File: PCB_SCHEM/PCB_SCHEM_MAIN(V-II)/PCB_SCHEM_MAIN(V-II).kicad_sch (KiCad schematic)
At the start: 0 parts

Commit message: Schem Update
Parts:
- added U1: RP2040, Package_DFN_QFN:QFN-56-1EP_7x7mm_P0.4mm_EP3.2x3.2mm, symbol MCU_RaspberryPi:RP2040
- added U2: TPS61291DRVR, DRV0006A, symbol 2026-10-14_05-55-56:TPS61291DRVR
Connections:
- new net: U1.1 (IOVDD), U1.10 (IOVDD), U1.22 (IOVDD), U1.33 (IOVDD), U1.42 (IOVDD), U1.49 (IOVDD)
- new net: U1.23 (DVDD), U1.50 (DVDD)

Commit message: Added all the IC's, the main framework of the PCB done. Minor wiring and final touches left
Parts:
- added BT1: Battery_Cell, Package_SON:Texas_DRC0010J_ThermalVias, symbol Device:Battery_Cell
- added C1, C2: 22pf, Package_SO:SOIC-8_3.9x4.9mm_P1.27mm, symbol Device:C_Small
- added C3: 100nf, Package_SO:SOIC-8_3.9x4.9mm_P1.27mm, symbol Device:C_Small
- added D1: SS14, Diode_SMD:D_SMA, symbol Diode:SS14
- added D2: D, Diode_SMD:D_SMA, symbol Device:D
- added J1: USB_C_Receptacle_USB2.0_14P, Package_DFN_QFN:WDFN-10-1EP_3x3mm_P0.5mm_EP1.8x2.5mm, symbol Connector:USB_C_Receptacle_USB2.0_14P
- added L1: L_Ferrite_Small, Package_BGA:BGA-624_21x21mm_Layout25x25_P0.8mm, symbol Device:L_Ferrite_Small
- added R1: R, Package_DIP:DIP-8_W7.62mm, symbol Device:R
- added R2: 10K, Package_DIP:DIP-8_W7.62mm, symbol Device:R
- added R3, R4: 5K1, Package_DIP:DIP-8_W7.62mm, symbol Device:R
- added U3: LSM6DS3, Package_LGA:LGA-14_3x2.5mm_P0.5mm_LayoutBorder3x4y, symbol Sensor_Motion:LSM6DS3
- added U4, U5: MX25L3233FM1, Package_SO:JEITA_SOIC-8_3.9x4.9mm_P1.27mm, symbol Memory_Flash:MX25L3233FM1
- added Y1: Crystal, Package_SO:JEITA_SOIC-8_3.9x4.9mm_P1.27mm, symbol Device:Crystal
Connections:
- net at U2.1 (L): now also L1.2
- net 3.3V: now reaches U2.2 (VOUT)
- net 3.3V: now also U1.1 (IOVDD), U1.10 (IOVDD), U1.22 (IOVDD), U1.33 (IOVDD), U1.42 (IOVDD), U1.43 (ADC_AVDD), U1.44 (VREG_VIN), U1.48 (USB_VDD), U1.49 (IOVDD), U2.5 (VSEL), C3.2, U3.5 (VDDIO), U3.8 (VDD), U4.8 (VCC), U5.8 (VCC)
- net VIN: now reaches U2.3 (VIN)
- net VIN: now also D1.1 (K), D2.1 (K), L1.1, R1.1
- net at U2.4 (EN_BYP): now also U1.37 (GPIO25), R1.2
- net GND: now reaches U2.6 (GND)
- net GND: now also U1.3 (GPIO1), U1.57 (GND), U2.7 (PAD), BT1.2 (-), C3.1, J1.A1 (GND), J1.A12 (GND), J1.B1 (GND), J1.B12 (GND), J1.SH (SHIELD), R2.2, R3.2, R4.2, U3.6 (GND), U3.7 (GND), U4.4 (GND)
- net at U1.16 (GPIO13): now also U5.1 (~{CS})
- net at U1.17 (GPIO14): now also U5.6 (SCLK)
- net at U1.2 (GPIO0): now also U3.1 (SDO/SA0)
- net at U1.20 (XIN): now also C1.1
- net at U1.21 (XOUT): now also C2.2
- net at U1.23 (DVDD), U1.50 (DVDD): now also U1.45 (VREG_VOUT)
- net at U1.35 (GPIO23): now also U3.9 (INT2)
- net at U1.36 (GPIO24): now also U3.4 (INT1)
- net at U1.4 (GPIO2): now also U3.13 (SCL)
- net at U1.46 (USB_DM): now also J1.A7 (D-), J1.B7 (D-)
- net at U1.47 (USB_DP): now also J1.A6 (D+), J1.B6 (D+)
- net at U1.5 (GPIO3): now also U3.14 (SDA)
- net at U1.51 (QSPI_SD3): now also U4.7 (~{HOLD}/SIO3)
- net at U1.52 (QSPI_SCLK): now also U4.6 (SCLK)
- net at U1.53 (QSPI_SD0): now also U4.5 (SI/SIO0)
- net at U1.54 (QSPI_SD2): now also U4.3 (~{WP}/SIO2)
- net at U1.55 (QSPI_SD1): now also U4.2 (SO/SIO1)
- net at U1.56 (~{QSPI_SS}): now also U4.1 (~{CS})
- new net: J1.A5 (CC1), R3.1
- new net: D1.2 (A), J1.A4 (VBUS), J1.A9 (VBUS), J1.B4 (VBUS), J1.B9 (VBUS)
- new net: J1.B5 (CC2), R4.1
- new net: R2.1, U3.12 (CS)
- new net: C1.2, Y1.1
- new net: BT1.1 (+), D2.2 (A)
- new net: C2.1, Y1.2
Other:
- moved on the sheet: U1, U2

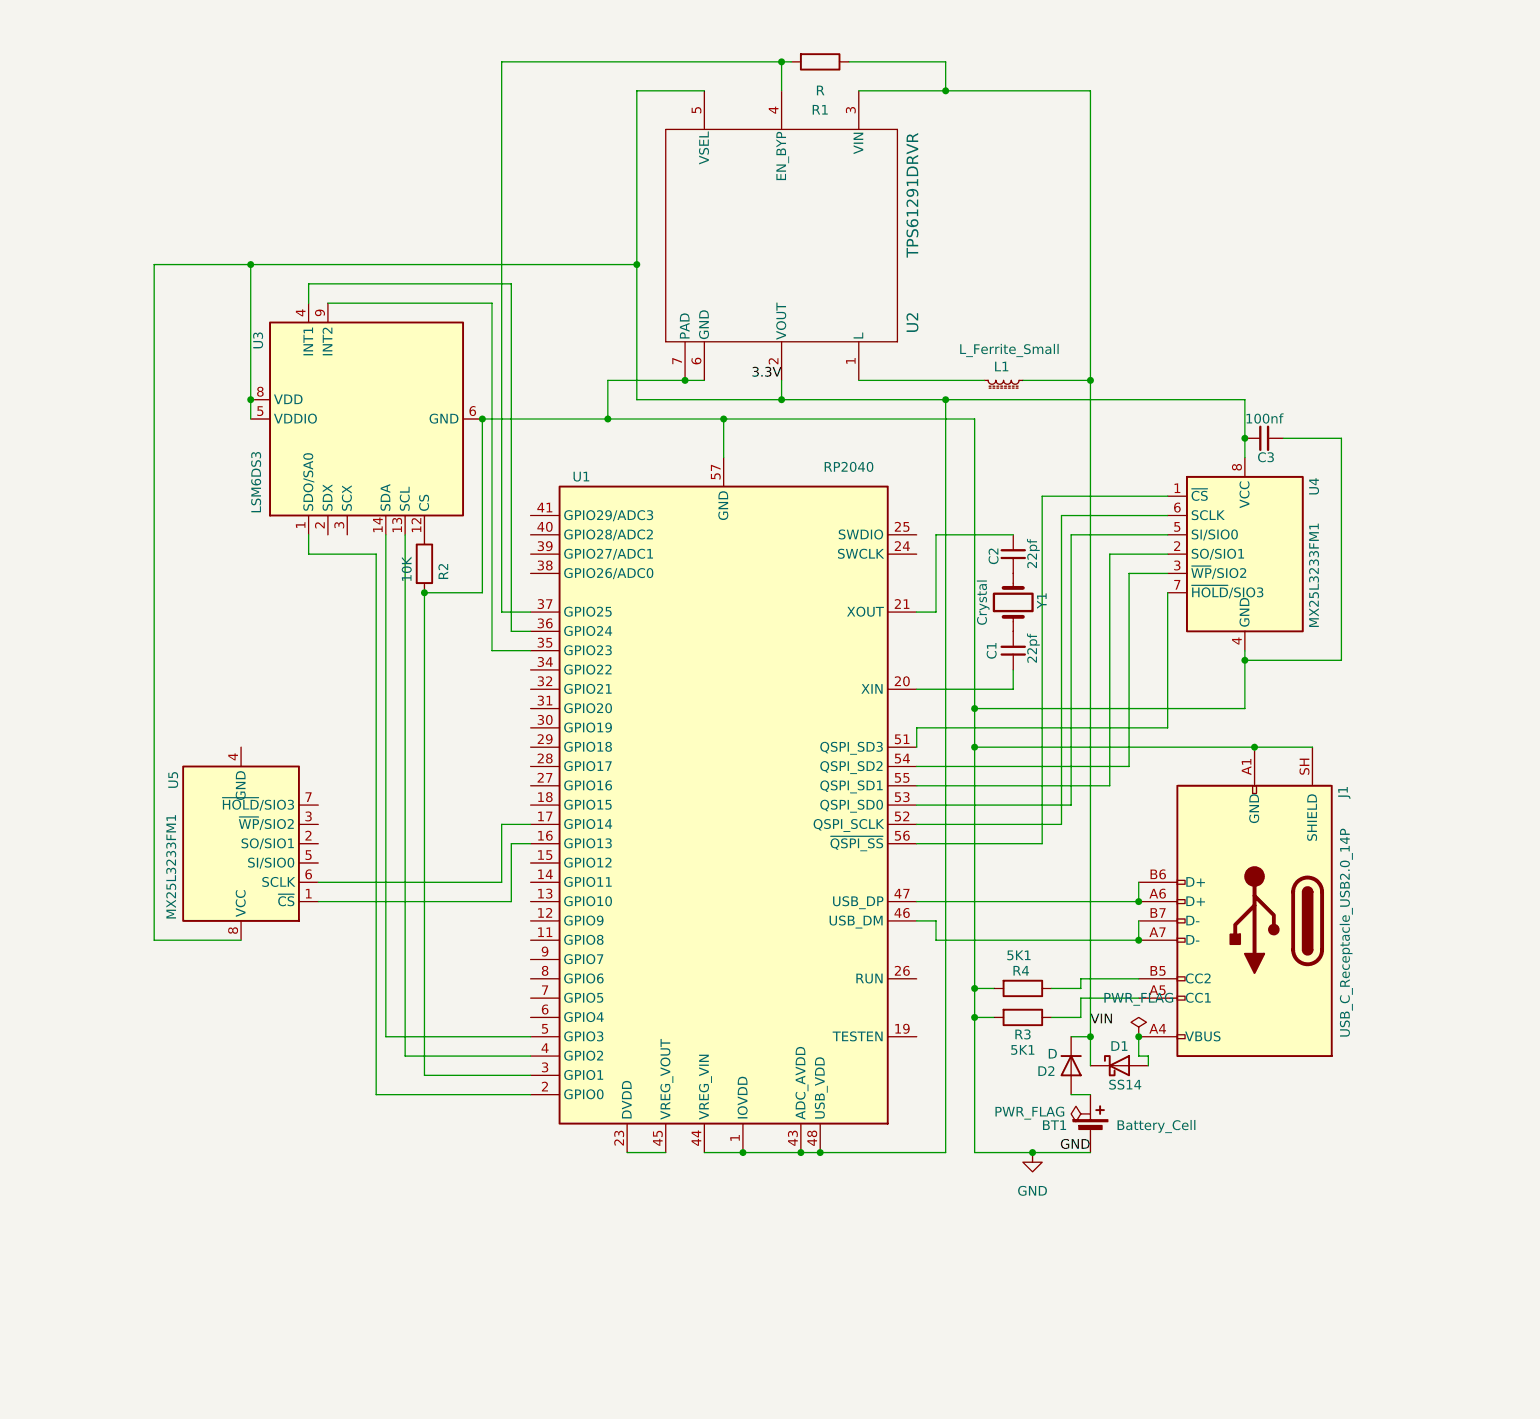
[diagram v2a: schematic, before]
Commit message: Completed Schematic design, and imported footprints to the PCB editor.
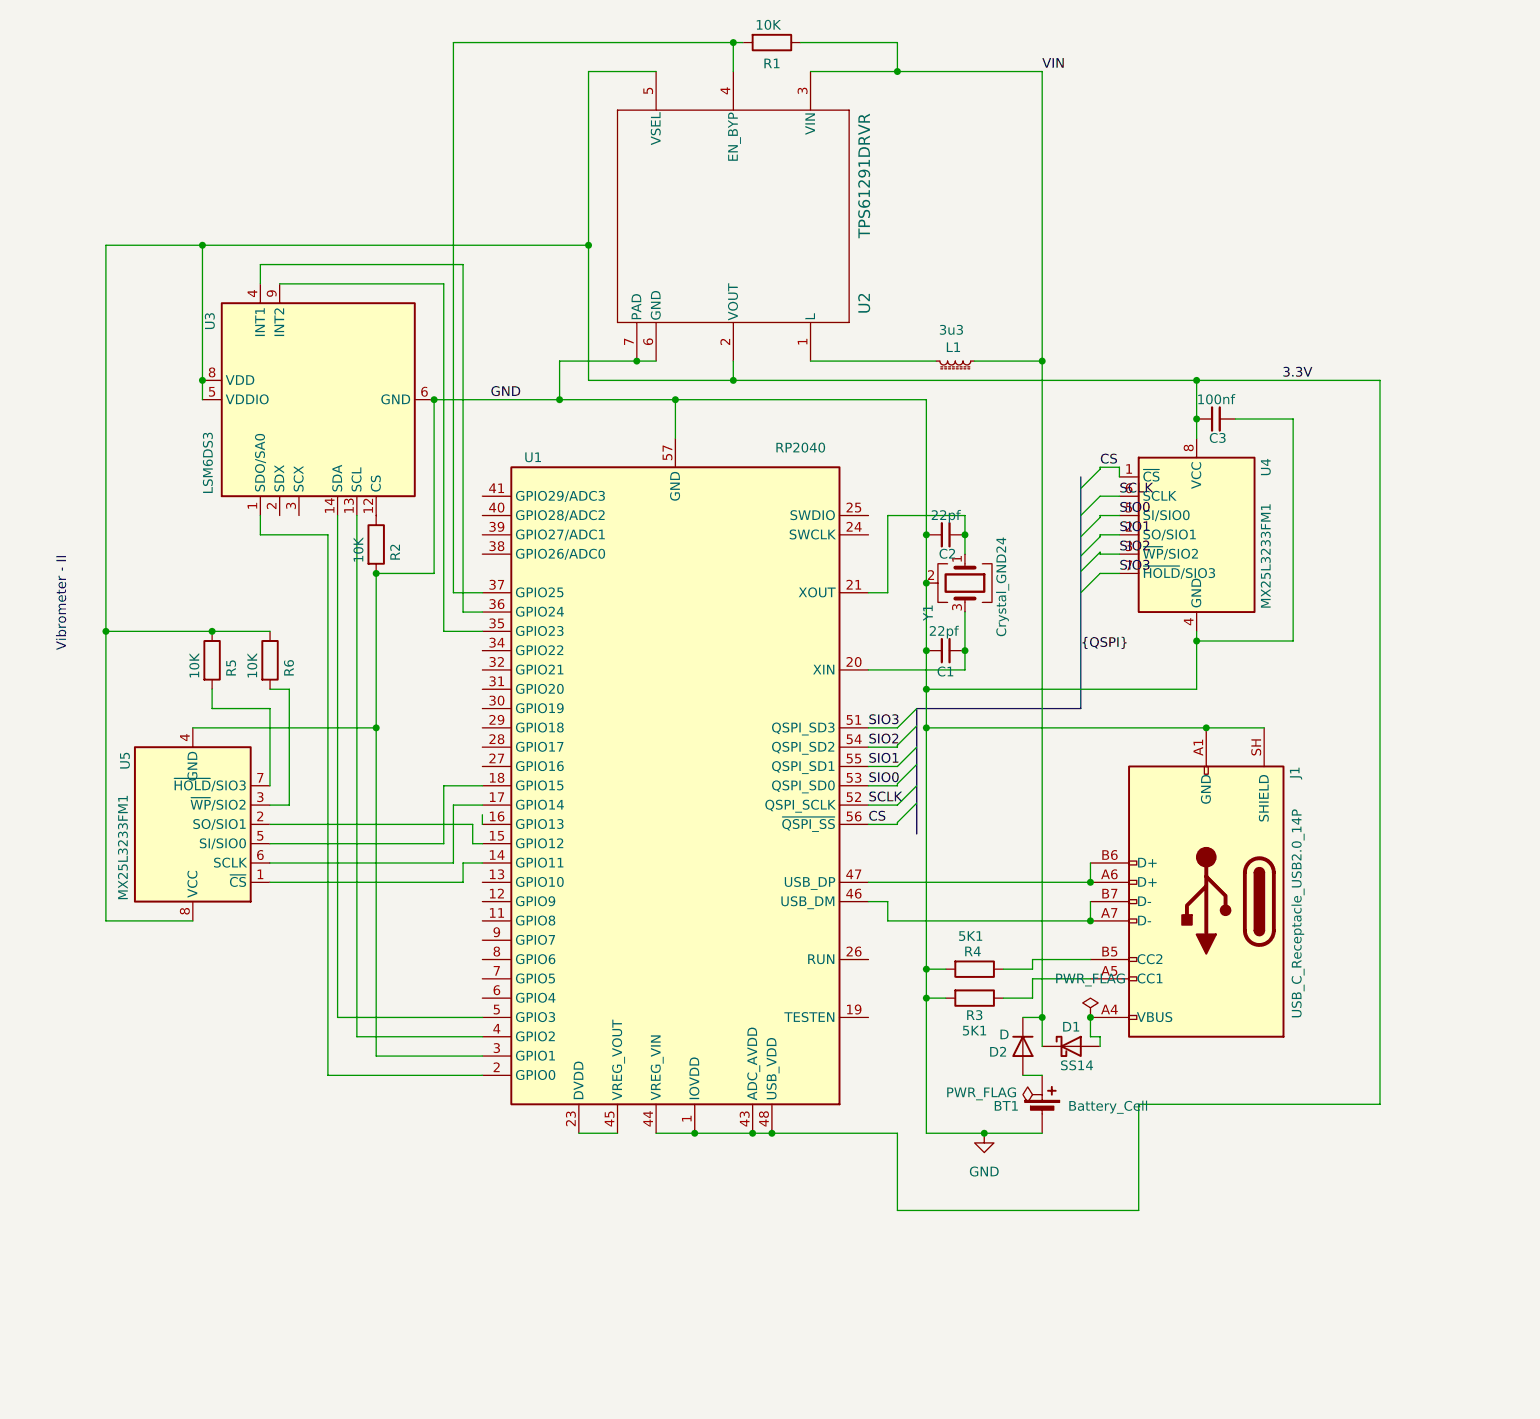
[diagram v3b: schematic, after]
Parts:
- removed Y1: Crystal, Package_SO:JEITA_SOIC-8_3.9x4.9mm_P1.27mm, symbol Device:Crystal
- added R5, R6: 10K, Resistor_SMD:R_0603_1608Metric_Pad0.98x0.95mm_HandSolder, symbol Device:R
- added Y1: Crystal_GND24, Crystal:Crystal_SMD_Abracon_ABM8AIG-4Pin_3.2x2.5mm, symbol Device:Crystal_GND24
- BT1: footprint Package_SON:Texas_DRC0010J_ThermalVias -> Battery:BatteryHolder_MYOUNG_BS-07-A1BJ001_CR2032
- C1, C2, C3: footprint Package_SO:SOIC-8_3.9x4.9mm_P1.27mm -> Capacitor_SMD:C_0603_1608Metric_Pad1.08x0.95mm_HandSolder
- J1: footprint Package_DFN_QFN:WDFN-10-1EP_3x3mm_P0.5mm_EP1.8x2.5mm -> Connector_USB:USB_C_Receptacle_GCT_USB4105-xx-A_16P_TopMnt_Horizontal
- L1: value L_Ferrite_Small -> 3u3; footprint Package_BGA:BGA-624_21x21mm_Layout25x25_P0.8mm -> Inductor_SMD:L_Coilcraft_LPS3010
- R1: value R -> 10K; footprint Package_DIP:DIP-8_W7.62mm -> Resistor_SMD:R_0603_1608Metric_Pad0.98x0.95mm_HandSolder
- R2, R3, R4: footprint Package_DIP:DIP-8_W7.62mm -> Resistor_SMD:R_0603_1608Metric_Pad0.98x0.95mm_HandSolder
- U2: footprint DRV0006A -> Package_SON:WSON-6-1EP_2x2mm_P0.65mm_EP1x1.6mm_ThermalVias
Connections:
- net 3.3V: now also R5.1, R6.1
- net GND: now also C1.2, C2.2, U5.4 (GND), Y1.2 (G), Y1.4 (G)
- net at C1.1, U1.20 (XIN): now also Y1.3
- net CS: now reaches U1.56 (~{QSPI_SS}), U4.1 (~{CS})
- net SIO1: now reaches U1.55 (QSPI_SD1), U4.2 (SO/SIO1)
- net SIO2: now reaches U1.54 (QSPI_SD2), U4.3 (~{WP}/SIO2)
- net SIO0: now reaches U1.53 (QSPI_SD0), U4.5 (SI/SIO0)
- net SCLK: now reaches U1.52 (QSPI_SCLK), U4.6 (SCLK)
- net SIO3: now reaches U1.51 (QSPI_SD3), U4.7 (~{HOLD}/SIO3)
- net at U5.1 (~{CS}): now also U1.14 (GPIO11); no longer U1.16 (GPIO13)
- net at U5.2 (SO/SIO1): now also U1.15 (GPIO12)
- net at U5.3 (~{WP}/SIO2): now also R6.2
- net at U5.5 (SI/SIO0): now also U1.18 (GPIO15)
- net at U5.7 (~{HOLD}/SIO3): now also R5.2
- net at C2.1: now also U1.21 (XOUT), Y1.1
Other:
- note added: "Vibrometer - II"
- moved on the sheet: BT1, C1, C2, C3, D1, D2, J1, L1, R1, R2, R3, R4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

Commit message: PCB design and schematic fully completed. No further changes, maybe minor trace shifts at best. PCB step file is exported to Fusion, enclousre yet to be designed.
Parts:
- added C4, C5: 100nf, Capacitor_SMD:C_0603_1608Metric_Pad1.08x0.95mm_HandSolder, symbol Device:C_Small
- added R7, R8: 27, Resistor_SMD:R_0603_1608Metric_Pad0.98x0.95mm_HandSolder, symbol Device:R
- added R9: 1K, Resistor_SMD:R_0603_1608Metric_Pad0.98x0.95mm_HandSolder, symbol Device:R
- added SW1: SW_Push, Button_Switch_SMD:SW_SPST_EVQP2_MiddlePushTravel_H2.5mm, symbol Switch:SW_Push
- U2: footprint Package_SON:WSON-6-1EP_2x2mm_P0.65mm_EP1x1.6mm_ThermalVias -> Package_SON:WSON-6-1EP_2x2mm_P0.65mm_EP1x1.6mm
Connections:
- net 3.3V: now also C4.2, C5.1
- net CS: now also R9.2
- net GND: now also C4.1, C5.2, SW1.1
- net D+: now reaches J1.A6 (D+), J1.B6 (D+)
- net D+: now also R7.1; no longer U1.47 (USB_DP)
- net D-: now reaches J1.A7 (D-), J1.B7 (D-)
- net D-: now also R8.1; no longer U1.46 (USB_DM)
- new net: R9.1, SW1.2
- new net MCU_DN: R8.2, U1.46 (USB_DM)
- new net MCU_DP: R7.2, U1.47 (USB_DP)
